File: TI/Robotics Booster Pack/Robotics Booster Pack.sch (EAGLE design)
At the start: 115 parts, among them J1 1X2.PTS, U1 TS3A44159.RGT, U10 74LVTH125.RGY, U11 SCHA4B0400, U12 BLUETOOTH-RN41", U13 XBEE-1XBEE-1_LOCK, U14 TPS5450, U15 TPS715XX.DCK, U16 TPS6215X.RGT, U3 DRV8800, U4 DRV8800, U5 DRV8800, U6 DRV8800, U7 PCA9557.RGV, U8 MPU-6050, U9 INA220.DGS

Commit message: More Robotics BP v2 routing. Power regulators routed and completed Most IO Expander signals completely routed
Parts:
- removed U$6: 1X4, headers(.1in):1X4
- U16: value TPS6215X.RGT -> TPS62152.RGT
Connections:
- removed net SVRO.EN: Q2.A.G, Q2.B.G, R8.1
- net 3.3V: no longer U$6.1
- net GND: now also C1.-; no longer U$6.4
- net I2C.SCL: no longer U$6.3
- net I2C.SDA: no longer U$6.2
- net SRVO.EN: now also Q2.A.G, Q2.B.G, R8.1
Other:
- moved on the sheet: C38
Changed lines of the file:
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@@
 <part name="U$45" library="microbuilder" deviceset="GND" device=""/>
 <part name="H9" library="headers(.1in)" deviceset="1X3" device=""/>
-<part name="U$13" library="microbuilder" deviceset="3.3V" device=""/>
-<part name="U$41" library="microbuilder" deviceset="GND" device=""/>
 <part name="J2" library="solderjumper" deviceset="SOLDERJUMPER.2" device=".MED"/>
 <part name="U$12" library="microbuilder" deviceset="3.3V" device=""/>
@@
 <part name="U$36" library="microbuilder" deviceset="VBAT" device=""/>
 <part name="U$37" library="microbuilder" deviceset="GND" device=""/>
-<part name="U$6" library="headers(.1in)" deviceset="1X4" device=""/>
 <part name="D1" library="comchip" deviceset="CDBMT____-HF" device="" value="CDBMT2100-HF"/>
 <part name="D3" library="comchip" deviceset="CDBMT____-HF" device="" value="CDBMT2100-HF"/>
@@
 <part name="C1" library="microbuilder" deviceset="CAP_ELECTROLYTIC" device="PANASONIC_D" value="100uF"/>
 <part name="U15" library="packages(ti)" deviceset="TPS715XX" device=".DCK"/>
-<part name="U16" library="packages(ti)" deviceset="TPS6215X" device=".RGT"/>
+<part name="U16" library="packages(ti)" deviceset="TPS6215X" device=".RGT" value="TPS62152.RGT"/>
 <part name="C10" library="standardparts" deviceset="CAPACITOR" device=".0603" value=".1uF"/>
 <part name="C11" library="standardparts" deviceset="CAPACITOR" device=".0603" value="1uF"/>
@@
 <instance part="U$124" gate="G$1" x="220.98" y="66.04"/>
 <instance part="U$125" gate="G$1" x="220.98" y="43.18"/>
-<instance part="U$98" gate="G$1" x="266.7" y="66.04"/>
-<instance part="U$127" gate="G$1" x="266.7" y="55.88"/>
-<instance part="C38" gate="G$1" x="266.7" y="60.96" rot="R270"/>
+<instance part="U$98" gate="G$1" x="254" y="66.04"/>
+<instance part="U$127" gate="G$1" x="254" y="55.88"/>
+<instance part="C38" gate="G$1" x="254" y="60.96" rot="R270"/>
 <instance part="LED1" gate="G$1" x="322.58" y="165.1"/>
 <instance part="LED2" gate="G$1" x="320.04" y="160.02"/>
@@
 <instance part="U$45" gate="G$1" x="78.74" y="177.8"/>
 <instance part="H9" gate="G$1" x="66.04" y="180.34"/>
-<instance part="U$13" gate="G$1" x="416.56" y="134.62"/>
-<instance part="U$41" gate="G$1" x="416.56" y="121.92"/>
 <instance part="J2" gate="G$1" x="269.24" y="132.08" smashed="yes" rot="R90">
 <attribute name="VALUE" x="271.78" y="130.81" size="1.016" layer="96" rot="R90"/>
@@
 <instance part="U$36" gate="G$1" x="60.96" y="35.56" rot="MR0"/>
 <instance part="U$37" gate="G$1" x="142.24" y="15.24" rot="R90"/>
-<instance part="U$6" gate="G$1" x="411.48" y="127"/>
 <instance part="D1" gate="G$1" x="15.24" y="233.68" smashed="yes" rot="MR90">
 <attribute name="NAME" x="17.014" y="233.66" size="1.016" layer="95" rot="MR90"/>
@@
 <wire x1="15.24" y1="233.68" x2="15.24" y2="231.14" width="0.1524" layer="91"/>
 <junction x="15.24" y="231.14"/>
+<pinref part="C1" gate="G$1" pin="-"/>
+<junction x="20.32" y="231.14"/>
 </segment>
 <segment>
@@
 </segment>
 <segment>
-<pinref part="U$41" gate="G$1" pin="GND"/>
-<wire x1="414.02" y1="124.46" x2="416.56" y2="124.46" width="0.1524" layer="91"/>
-<pinref part="U$6" gate="G$1" pin="4"/>
-</segment>
-<segment>
 <pinref part="H14" gate="G$1" pin="1"/>
 <pinref part="U$50" gate="G$1" pin="GND"/>
@@
 </segment>
 <segment>
-<pinref part="U$13" gate="G$1" pin="3.3V"/>
-<wire x1="414.02" y1="132.08" x2="416.56" y2="132.08" width="0.1524" layer="91"/>
-<pinref part="U$6" gate="G$1" pin="1"/>
-</segment>
-<segment>
 <pinref part="J2" gate="G$1" pin="2"/>
 <pinref part="U$12" gate="G$1" pin="3.3V"/>
@@
 <label x="195.58" y="17.78" size="1.27" layer="95" rot="MR0"/>
 </segment>
-<segment>
-<wire x1="414.02" y1="129.54" x2="421.64" y2="129.54" width="0.1524" layer="91"/>
-<label x="421.64" y="129.54" size="1.27" layer="95" rot="MR0"/>
-<pinref part="U$6" gate="G$1" pin="2"/>
-</segment>
 </net>
 <net name="I2C.SCL" class="0">
@@
 <wire x1="195.58" y1="15.24" x2="187.96" y2="15.24" width="0.1524" layer="91"/>
 <label x="195.58" y="15.24" size="1.27" layer="95" rot="MR0"/>
-</segment>
-<segment>
-<wire x1="421.64" y1="127" x2="414.02" y2="127" width="0.1524" layer="91"/>
-<label x="421.64" y="127" size="1.27" layer="95" rot="MR0"/>
-<pinref part="U$6" gate="G$1" pin="3"/>
 </segment>
 </net>
@@
 </segment>
 </net>
-<net name="SVRO.EN" class="0">
+<net name="SRVO.EN" class="0">
+<segment>
+<pinref part="U7" gate="G$1" pin="P2"/>
+<wire x1="238.76" y1="58.42" x2="248.92" y2="58.42" width="0.1524" layer="91"/>
+<label x="248.92" y="58.42" size="1.27" layer="95" rot="MR0"/>
+</segment>
+<segment>
+<pinref part="U10" gate="G$1" pin="3A"/>
+<wire x1="297.18" y1="152.4" x2="287.02" y2="152.4" width="0.1524" layer="91"/>
+<label x="287.02" y="152.4" size="1.27" layer="95"/>
+</segment>
 <segment>
 <pinref part="Q2" gate=".A" pin="G"/>
@@
 </segment>
 </net>
-<net name="SRVO.EN" class="0">
-<segment>
-<pinref part="U7" gate="G$1" pin="P2"/>
-<wire x1="238.76" y1="58.42" x2="248.92" y2="58.42" width="0.1524" layer="91"/>
-<label x="248.92" y="58.42" size="1.27" layer="95" rot="MR0"/>
-</segment>
-<segment>
-<pinref part="U10" gate="G$1" pin="3A"/>
-<wire x1="297.18" y1="152.4" x2="287.02" y2="152.4" width="0.1524" layer="91"/>
-<label x="287.02" y="152.4" size="1.27" layer="95"/>
-</segment>
-</net>

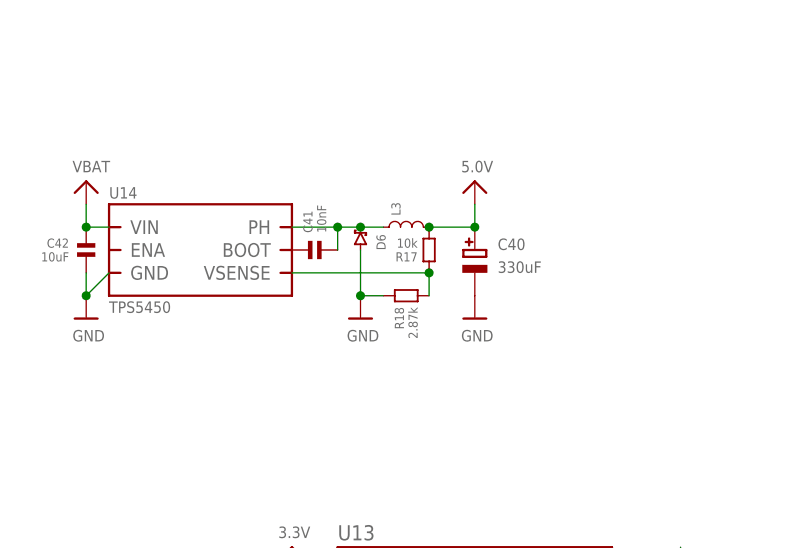
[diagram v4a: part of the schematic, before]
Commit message: Robotics BoosterPack v2 Complete! Still need to double check a few mote things, and clean up the silkscreen.
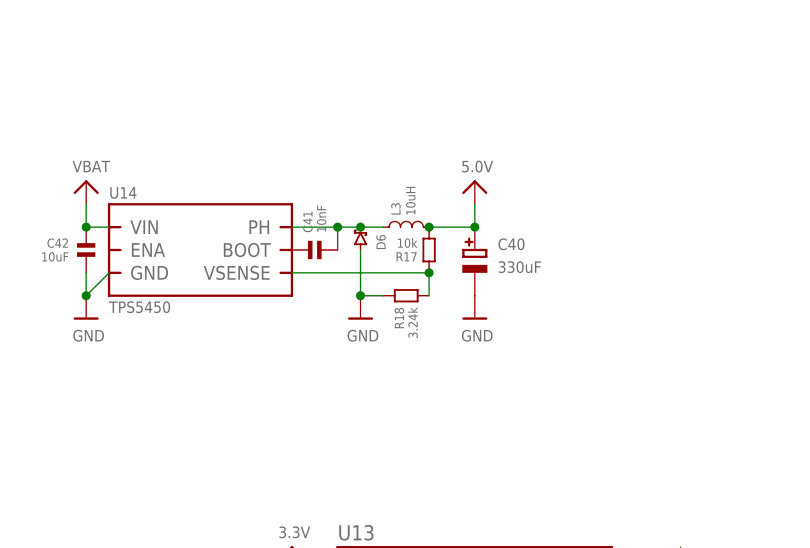
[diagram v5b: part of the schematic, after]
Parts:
- L3: value (none) -> 10uH
- R18: value 2.87k -> 3.24k
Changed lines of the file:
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@@
 <part name="U14" library="packages(ti)" deviceset="TPS54X0" device="" value="TPS5450"/>
 <part name="C40" library="microbuilder" deviceset="CAP_ELECTROLYTIC" device="PANASONIC_D" value="330uF"/>
-<part name="L3" library="coilcraft" deviceset="INDUCTOR" device=".XAL6060"/>
+<part name="L3" library="coilcraft" deviceset="INDUCTOR" device=".XAL6060" value="10uH"/>
 <part name="D6" library="comchip" deviceset="CDBC5XXX-G" device=""/>
 <part name="C41" library="standardparts" deviceset="CAPACITOR" device=".0603" value="10nF"/>
@@
 <part name="U$55" library="microbuilder" deviceset="VBAT" device=""/>
 <part name="R17" library="standardparts" deviceset="RESISTOR" device=".0603" value="10k"/>
-<part name="R18" library="standardparts" deviceset="RESISTOR" device=".0603" value="2.87k"/>
+<part name="R18" library="standardparts" deviceset="RESISTOR" device=".0603" value="3.24k"/>
 <part name="U$59" library="microbuilder" deviceset="GND" device=""/>
 <part name="U$61" library="microbuilder" deviceset="GND" device=""/>
@@
 <instance part="U14" gate="G$1" x="210.82" y="231.14"/>
 <instance part="C40" gate="G$1" x="241.3" y="228.6"/>
-<instance part="L3" gate="G$1" x="233.68" y="233.68" smashed="yes">
-<attribute name="NAME" x="233.045" y="234.95" size="1.016" layer="95" rot="R90"/>
-</instance>
+<instance part="L3" gate="G$1" x="233.68" y="233.68"/>
 <instance part="D6" gate="G$1" x="228.6" y="231.14" smashed="yes" rot="MR90">
 <attribute name="NAME" x="230.374" y="231.12" size="1.016" layer="95" rot="MR90"/>

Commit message: Cleaned up completed Robotics Booster Pack v2. Sent off to OSHPark!
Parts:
- J4: device solderjumper:SOLDERJUMPER.3.LRG.12 -> solderjumper:SOLDERJUMPER.3.LRG.23
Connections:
- net M0+: now also H17.1, U5.OUT-; no longer H17.2, U5.OUT+
- net M0-: now also H17.2, U5.OUT+; no longer H17.1, U5.OUT-
- net M1+: now also H18.1, U6.OUT-; no longer H18.2, U6.OUT+
- net M1-: now also H18.2, U6.OUT+; no longer H18.1, U6.OUT-
- net M2+: now also H19.1, U3.OUT-; no longer H19.2, U3.OUT+
- net M2-: now also H19.2, U3.OUT+; no longer H19.1, U3.OUT-
- net M3+: now also H20.1, U4.OUT-; no longer H20.2, U4.OUT+
- net M3-: now also H20.2, U4.OUT+; no longer H20.1, U4.OUT-
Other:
- note removed: "NOTES: - Change headers to Samtec Parts - Update Rn-41/2 Footprint"
- moved on the sheet: C12, C13, C14, C20, C22, C32, C33, C34, C36, C37, C38, C39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

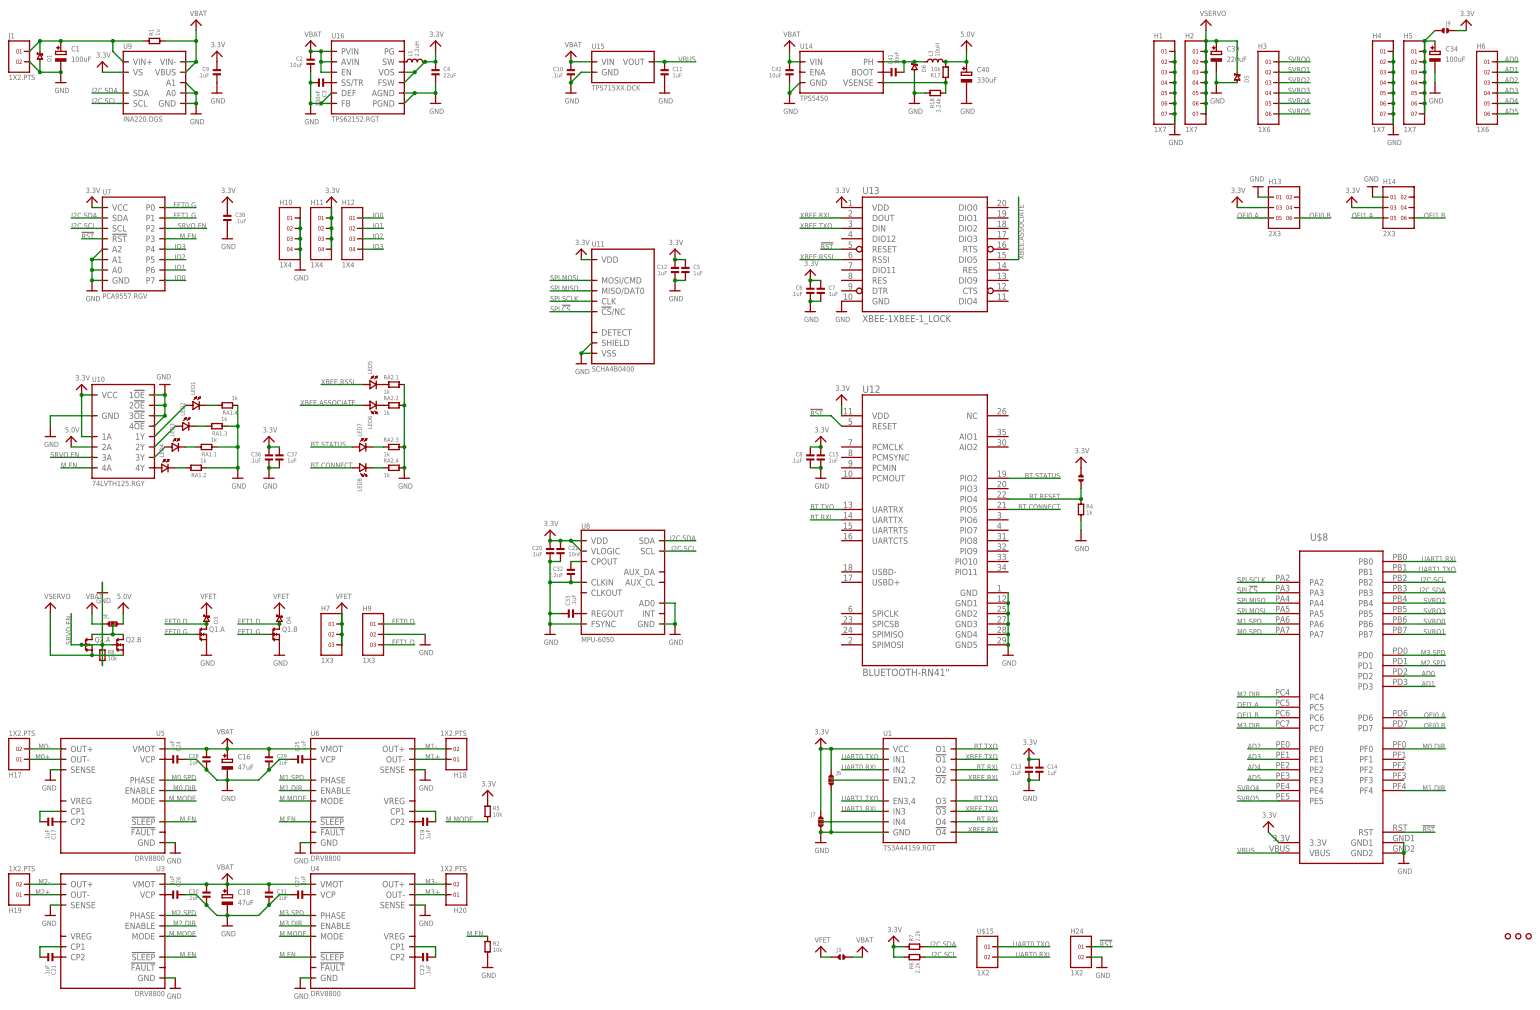
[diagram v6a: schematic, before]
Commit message: Cleaned up part names
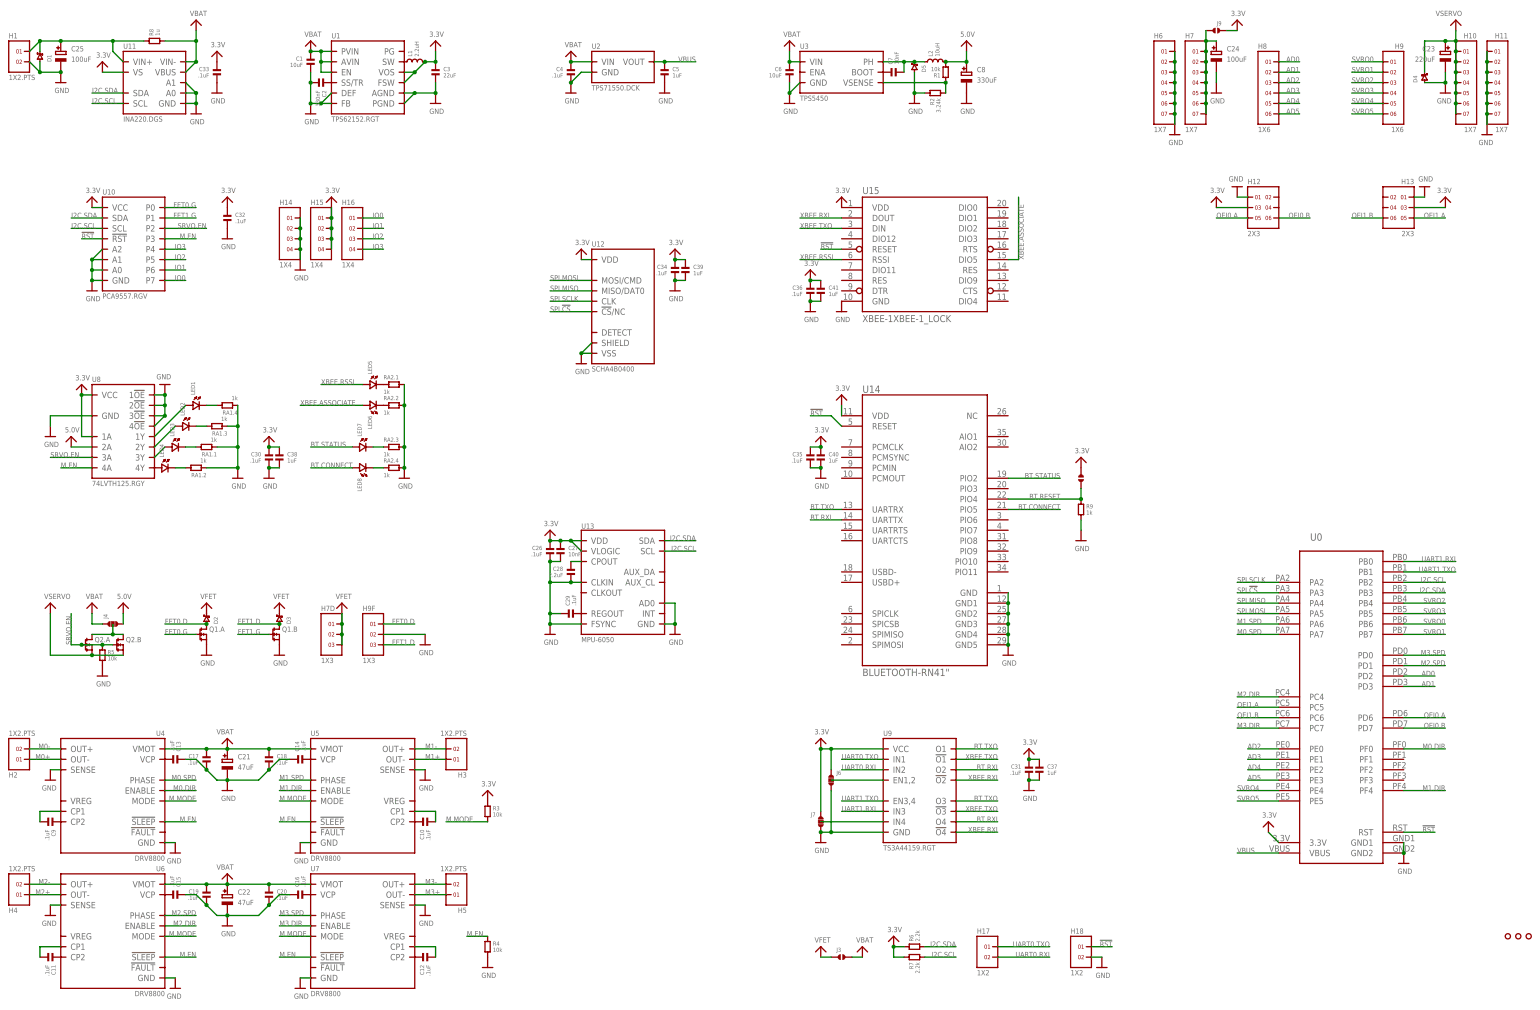
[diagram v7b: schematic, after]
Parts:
- removed C42: 10uF, standardparts:CAPACITOR.1206
- removed D6: CDBC5XXX-G, comchip:CDBC5XXX-G
- removed H19, H20, J1: 1X2.PTS, phoenixcontact:1X2.PTS.PLUG
- removed H24, U$15: 1X2, headers(.1in):1X2
- removed R17: 10k, standardparts:RESISTOR.0603
- removed R18: 3.24k, standardparts:RESISTOR.0603
- removed U16: TPS62152.RGT, packages(ti):TPS6215X.RGT
- added C35: .1uF, standardparts:CAPACITOR.0603
- added D2: CDBMT2100-HF, comchip:CDBMT____-HF
- added H15, H16: 1X4, headers(.1in):1X4
- added H7D, H9F: 1X3, headers(.1in):1X3
- added H8: 1X6, headers(.1in):1X6
- added R3: 10k, standardparts:RESISTOR.0603
- added R9: 1k, standardparts:RESISTOR.0603
- added U2: TPS71550.DCK, packages(ti):TPS715XX.DCK
- C1: value 100uF -> 10uF; device microbuilder:CAP_ELECTROLYTICPANASONIC_D -> standardparts:CAPACITOR.1206
- C11, C14, C15: value 1uF -> .1uF
- C16, C18: value 47uF -> .1uF; device microbuilder:CAP_ELECTROLYTICPANASONIC_D -> standardparts:CAPACITOR.0603
- C2: value 10uF -> 330nF; device standardparts:CAPACITOR.1206 -> standardparts:CAPACITOR.0603
- C21: value .1uF -> 47uF; device standardparts:CAPACITOR.0603 -> microbuilder:CAP_ELECTROLYTICPANASONIC_D
- C22: value 10nF -> 47uF; device standardparts:CAPACITOR.0603 -> microbuilder:CAP_ELECTROLYTICPANASONIC_D
- C23: value .1uF -> 220uF; device standardparts:CAPACITOR.0603 -> microbuilder:CAP_ELECTROLYTICPANASONIC_D
- C24, C25: value .1uF -> 100uF; device standardparts:CAPACITOR.0603 -> microbuilder:CAP_ELECTROLYTICPANASONIC_D
- C27: value .1uF -> 10nF
- C28: value .1uF -> 2.2uF
- C3: value 330nF -> 22uF; device standardparts:CAPACITOR.0603 -> standardparts:CAPACITOR.0805
- C32: value 2.2uF -> .1uF
- C34: value 100uF -> .1uF; device microbuilder:CAP_ELECTROLYTICPANASONIC_D -> standardparts:CAPACITOR.0603
- C38: value .1uF -> 1uF
- C39: value 220uF -> 1uF; device microbuilder:CAP_ELECTROLYTICPANASONIC_D -> standardparts:CAPACITOR.0603
- C4: value 22uF -> .1uF; device standardparts:CAPACITOR.0805 -> standardparts:CAPACITOR.0603
- C40: value 330uF -> 1uF; device microbuilder:CAP_ELECTROLYTICPANASONIC_D -> standardparts:CAPACITOR.0603
- C41: value 10nF -> 1uF
- C6: value .1uF -> 10uF; device standardparts:CAPACITOR.0603 -> standardparts:CAPACITOR.1206
- C7: value 1uF -> 10nF
- C8: value .1uF -> 330uF; device standardparts:CAPACITOR.0603 -> microbuilder:CAP_ELECTROLYTICPANASONIC_D
- D5: value CDBMT2100-HF -> CDBC540-G; device comchip:CDBMT____-HF -> comchip:CDBC5XXX-G
- H1, H2, H4, H5: value 1X7 -> 1X2.PTS; device headers(.1in):1X7 -> phoenixcontact:1X2.PTS.PLUG
- H10, H11: value 1X4 -> 1X7; device headers(.1in):1X4 -> headers(.1in):1X7
- H12: value 1X4 -> 2X3; device headers(.1in):1X4 -> headers(.1in):2X3
- H14: value 2X3 -> 1X4; device headers(.1in):2X3 -> headers(.1in):1X4
- H17, H18: value 1X2.PTS -> 1X2; device phoenixcontact:1X2.PTS.PLUG -> headers(.1in):1X2
- H3: value 1X6 -> 1X2.PTS; device headers(.1in):1X6 -> phoenixcontact:1X2.PTS.PLUG
- H6: value 1X6 -> 1X7; device headers(.1in):1X6 -> headers(.1in):1X7
- H7: value 1X3 -> 1X7; device headers(.1in):1X3 -> headers(.1in):1X7
- H9: value 1X3 -> 1X6; device headers(.1in):1X3 -> headers(.1in):1X6
- Q1, Q2: value (none) -> FDMA3028N
- R1: value 1u -> 10k; device vishay:RESISTOR.WSK -> standardparts:RESISTOR.0603
- R2: value 10k -> 3.24k
- R4: value 1k -> 10k
- R8: value 10k -> 1u; device standardparts:RESISTOR.0603 -> vishay:RESISTOR.WSK
- U1: value TS3A44159.RGT -> TPS62152.RGT; device packages(ti):TS3A44159.RGT -> packages(ti):TPS6215X.RGT
- U10: value 74LVTH125.RGY -> PCA9557.RGV; device packages(ti):74XX125.RGY -> packages(ti):PCA9557.RGV
- U11: value SCHA4B0400 -> INA220.DGS; device alps:SCHA4B0400 -> packages(ti):INA220.DGS
- U12: value BLUETOOTH-RN41" -> SCHA4B0400; device SparkFun-RF:BLUETOOTH-RN41" -> alps:SCHA4B0400
- U13: value XBEE-1XBEE-1_LOCK -> MPU-6050; device SparkFun-RF:XBEE-1XBEE-1_LOCK -> invensense:MPU-6050
- U14: value TPS5450 -> BLUETOOTH-RN41"; device packages(ti):TPS54X0 -> SparkFun-RF:BLUETOOTH-RN41"
- U15: value TPS715XX.DCK -> XBEE-1XBEE-1_LOCK; device packages(ti):TPS715XX.DCK -> SparkFun-RF:XBEE-1XBEE-1_LOCK
- U3: value DRV8800 -> TPS5450; device packages(ti):DRV8800.RTY -> packages(ti):TPS54X0
- U7: value PCA9557.RGV -> DRV8800; device packages(ti):PCA9557.RGV -> packages(ti):DRV8800.RTY
- U8: value MPU-6050 -> 74LVTH125.RGY; device invensense:MPU-6050 -> packages(ti):74XX125.RGY
- U9: value INA220.DGS -> TS3A44159.RGT; device packages(ti):INA220.DGS -> packages(ti):TS3A44159.RGT
- renumbered L3 to L2, U$8 to U0
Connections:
- net !RST: now also H18.1, U10.!RST, U14.RESET, U15.RESET; no longer H24.1, U12.RESET, U13.RESET, U7.!RST
- net 3.3V: now also C26.1, C27.1, C3.1, C30.1, C31.1, C32.1, C33.1, C34.1, C35.1, C39.1, C40.1, C41.1, H12.3, H15.1, H15.2, H15.3, H15.4, R3.1, U1.FSW, U1.VOS, U11.VS, U13.VLOGIC, U14.VDD, U15.VDD, U8.1A, U8.VCC, U9.VCC; no longer C12.1, C13.1, C14.1, C15.1, C20.1, C22.1, C4.1, C5.1, C6.1, C7.1, C8.1, C9.1, H11.1, H11.2, H11.3, H11.4, H14.3, R5.1, U1.VCC, U10.1A, U11.VDD, U16.FSW, U16.VOS, U7.VCC, U8.VDD, U8.VLOGIC, U9.VS
- net 5.0V: now also C8.+, R1.2, U8.2A; no longer C40.+, R17.2, U10.2A
- net AD0: now also H8.1; no longer H6.1
- net AD1: now also H8.2; no longer H6.2
- net AD2: now also H8.3; no longer H6.3
- net AD3: now also H8.4; no longer H6.4
- net AD4: now also H8.5; no longer H6.5
- net AD5: now also H8.6; no longer H6.6
- net BT.CONNECT: now also U14.PIO5; no longer U12.PIO5
- net BT.RESET: now also R9.1, U14.PIO4; no longer R4.1, U12.PIO4
- net BT.RXI: now also U14.UARTTX, U9.O2, U9.O4; no longer U1.O2, U1.O4, U12.UARTTX
- net BT.STATUS: now also U14.PIO2; no longer U12.PIO2
- net BT.TXO: now also U14.UARTRX, U9.O1, U9.O3; no longer U1.O1, U1.O3, U12.UARTRX
- net FET0.D: now also D2.2, H9F.1; no longer D3.2, H9.1
- net FET0.G: now also U10.P0; no longer U7.P0
- net FET1.D: now also D3.2, H9F.3; no longer D4.2, H9.3
- net FET1.G: now also U10.P1; no longer U7.P1
- net GND: now also C1.2, C13.1, C14.1, C15.1, C16.1, C17.2, C18.2, C19.2, C21.-, C22.-, C23.-, C24.-, C25.-, C26.2, C27.2, C29.1, C33.2, C34.2, C35.2, C39.2, C40.2, C41.2, C8.-, D4.2, H11.1, H11.2, H11.3, H11.4, H11.5, H11.6, H11.7, H12.1, H14.2, H14.3, H14.4, H18.2, H6.1, H6.2, H6.3, H6.4, H6.5, H6.6, H6.7, H9F.2, R2.1, R5.2, R9.2, U1.AGND, U1.DEF, U1.FB, U1.PGND, U10.A0, U10.A1, U10.A2, U11.A0, U11.A1, U11.GND, U12.SHIELD, U12.VSS, U13.AD0, U13.CLKIN, U13.FSYNC, U14.GND1, U14.GND2, U14.GND3, U14.GND4, U14.GND5, U2.GND, U7.SENSE, U8.1!OE, U8.2!OE, U8.3!OE, U8.4!OE; no longer C1.-, C10.2, C11.2, C12.2, C13.2, C14.2, C15.2, C16.-, C18.-, C22.2, C24.1, C25.1, C26.1, C27.1, C29.2, C33.1, C34.-, C39.-, C40.-, C42.2, C7.2, C8.2, C9.2, D6.2, H1.1, H1.3, H1.4, H1.5, H1.6, H1.7, H10.1, H10.2, H10.3, H10.4, H24.2, H4.1, H4.2, H4.3, H4.4, H4.5, H4.6, H4.7, H9.2, J1.2, R18.1, R2.2, R8.2, U1.GND, U10.1!OE, U10.2!OE, U10.3!OE, U10.4!OE, U11.SHIELD, U11.VSS, U12.GND, U12.GND1, U12.GND2, U12.GND3, U12.GND4, U12.GND5, U16.AGND, U16.DEF, U16.FB, U16.PGND, U3.SENSE, U7.A0, U7.A1, U7.A2, U8.AD0, U8.CLKIN, U8.FSYNC, U9.A0, U9.A1
- net I2C.SCL: now also R7.2, U10.SCL, U11.SCL, U13.SCL; no longer R6.2, U7.SCL, U8.SCL, U9.SCL
- net I2C.SDA: now also R6.2, U10.SDA, U11.SDA, U13.SDA; no longer R7.2, U7.SDA, U8.SDA, U9.SDA
- net IO0: now also H16.1, U10.P7; no longer H12.1, U7.P7
- net IO1: now also H16.2, U10.P6; no longer H12.2, U7.P6
- net IO2: now also H16.3, U10.P5; no longer H12.3, U7.P5
- net IO3: now also H16.4, U10.P4; no longer H12.4, U7.P4
- net M.EN: now also R4.1, U10.P3, U7.!SLEEP, U8.4A; no longer R2.1, U10.4A, U3.!SLEEP, U7.P3
- net M.MODE: now also R3.2, U7.MODE; no longer R5.2, U3.MODE
- net M0+: now also H2.1, U4.OUT-; no longer H17.1, U5.OUT-
- net M0-: now also H2.2, U4.OUT+; no longer H17.2, U5.OUT+
- net M0.DIR: now also U4.ENABLE; no longer U5.ENABLE
- net M0.SPD: now also U4.PHASE; no longer U5.PHASE
- net M1+: now also H3.1, U5.OUT-; no longer H18.1, U6.OUT-
- net M1-: now also H3.2, U5.OUT+; no longer H18.2, U6.OUT+
- net M1.DIR: now also U5.ENABLE; no longer U6.ENABLE
- net M1.SPD: now also U5.PHASE; no longer U6.PHASE
- net M2+: now also H4.1, U6.OUT-; no longer H19.1, U3.OUT-
- net M2-: now also H4.2, U6.OUT+; no longer H19.2, U3.OUT+
- net M2.DIR: now also U6.ENABLE; no longer U3.ENABLE
- net M2.SPD: now also U6.PHASE; no longer U3.PHASE
- net M3+: now also H5.1, U7.OUT-; no longer H20.1, U4.OUT-
- net M3-: now also H5.2, U7.OUT+; no longer H20.2, U4.OUT+
- net M3.DIR: now also U7.ENABLE; no longer U4.ENABLE
- net M3.SPD: now also U7.PHASE; no longer U4.PHASE
- net N$1: now also U1.SW; no longer U16.SW
- net N$10: now also U8.2Y; no longer U10.2Y
- net N$11: now also U8.1Y; no longer U10.1Y
- net N$13: now also C9.1, U4.CP2; no longer C17.1, U5.CP2
- net N$18: now also C13.2, U4.VCP; no longer C24.2, U5.VCP
- net N$19: now also C14.2, U5.VCP; no longer C25.2, U6.VCP
- net N$2: now also U9.EN1,2; no longer U1.EN1,2
- net N$20: now also C15.2, U6.VCP; no longer C26.2, U3.VCP
- net N$21: now also C16.2, U7.VCP; no longer C27.2, U4.VCP
- net N$22: now also C25.+, H1.1, R8.1, U11.VIN+; no longer C1.+, J1.1, R1.1, U9.VIN+
- net N$23: now also C2.1, U1.SS/TR; no longer C3.1, U16.SS/TR
- net N$24: now also C28.1, U13.CPOUT; no longer C32.1, U8.CPOUT
- net N$25: now also C10.1, U5.CP2; no longer C19.1, U6.CP2
- net N$27: now also C11.1, U6.CP2; no longer C21.1, U3.CP2
- net N$29: now also C12.1, U7.CP2; no longer C23.1, U4.CP2
- net N$3: now also U9.IN4; no longer U1.IN4
- net N$32: now also U8.3Y; no longer U10.3Y
- net N$33: now also C7.1, U3.BOOT; no longer C41.1, U14.BOOT
- net N$34: now also C7.2, D5.1, U3.PH; no longer C41.2, D6.1, U14.PH
- net N$35: now also R1.1, R2.2, U3.VSENSE; no longer R17.1, R18.2, U14.VSENSE
- net N$37: now also C11.2, U6.CP1; no longer C21.2, U3.CP1
- net N$38: now also C9.2, U4.CP1; no longer C17.2, U5.CP1
- net N$39: now also C10.2, U5.CP1; no longer C19.2, U6.CP1
- net N$4: now also C24.+, H7.1, H7.2, H7.3, H7.4, H7.5, H7.6, H7.7; no longer C34.+, H5.1, H5.2, H5.3, H5.4, H5.5, H5.6, H5.7
- net N$40: now also C12.2, U7.CP1; no longer C23.2, U4.CP1
- net N$6: now also U8.4Y; no longer U10.4Y
- net N$7: now also C29.2, U13.REGOUT; no longer C33.2, U8.REGOUT
- net QEI0.A: now also H12.5; no longer H13.5
- net QEI0.B: now also H12.6; no longer H13.6
- net QEI1.A: now also H13.5; no longer H14.5
- net QEI1.B: now also H13.6; no longer H14.6
- net SPI.!CS: now also U12.!CS!/NC; no longer U11.!CS!/NC
- net SPI.MISO: now also U12.MISO/DAT0; no longer U11.MISO/DAT0
- net SPI.MOSI: now also U12.MOSI/CMD; no longer U11.MOSI/CMD
- net SPI.SCLK: now also U12.CLK; no longer U11.CLK
- net SRVO.EN: now also R5.1, U10.P2, U8.3A; no longer R8.1, U10.3A, U7.P2
- net SVRO0: now also H9.1; no longer H3.1
- net SVRO1: now also H9.2; no longer H3.2
- net SVRO2: now also H9.3; no longer H3.3
- net SVRO3: now also H9.4; no longer H3.4
- net SVRO4: now also H9.5; no longer H3.5
- net SVRO5: now also H9.6; no longer H3.6
- net UART0.RXI: now also H17.2, U9.IN2; no longer U$15.2, U1.IN2
- net UART0.TXO: now also H17.1, U9.IN1; no longer U$15.1, U1.IN1
- net UART1.RXI: now also U9.IN3; no longer U1.IN3
- net UART1.TXO: now also U9.EN3,4; no longer U1.EN3,4
- net VBAT: now also C1.1, C17.1, C18.1, C19.1, C20.1, C21.+, C22.+, C4.1, C6.1, R8.2, U1.AVIN, U1.EN, U1.PVIN, U11.VBUS, U11.VIN-, U2.VIN, U3.VIN, U7.VMOT; no longer C10.1, C16.+, C18.+, C2.1, C28.1, C29.1, C30.1, C31.1, C42.1, R1.2, U14.VIN, U15.VIN, U16.AVIN, U16.EN, U16.PVIN, U3.VMOT, U9.VBUS, U9.VIN-
- net VBUS: now also C5.1, U2.VOUT; no longer C11.1, U15.VOUT
- net VFET: now also D2.1, H7D.1, H7D.2, H7D.3; no longer D4.1, H7.1, H7.2, H7.3
- net VSERVO: now also C23.+, D4.1, H10.1, H10.2, H10.3, H10.4, H10.5, H10.6, H10.7; no longer C39.+, D5.1, H2.1, H2.2, H2.3, H2.4, H2.5, H2.6, H2.7
- net XBEE.ASSOCIATE: now also U15.DIO5; no longer U13.DIO5
- net XBEE.RSSI: now also U15.RSSI; no longer U13.RSSI
- net XBEE.RXI: now also U15.DOUT, U9.!O2, U9.!O4; no longer U1.!O2, U1.!O4, U13.DOUT
- net XBEE.TXO: now also U15.DIN, U9.!O1, U9.!O3; no longer U1.!O1, U1.!O3, U13.DIN
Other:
- moved on the sheet: C10, C11, C12, C13, C14, C15, C17, C19, C2, C20, C26, C27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
